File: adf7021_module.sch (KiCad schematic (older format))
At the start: 67 parts, among them J1 Conn_02x10_Counter_Clockwise, J2 Conn_Coaxial, J3 Conn_Coaxial, J4 Conn_02x10_Counter_Clockwise, U1 ADF7021, X1 19.68MHz

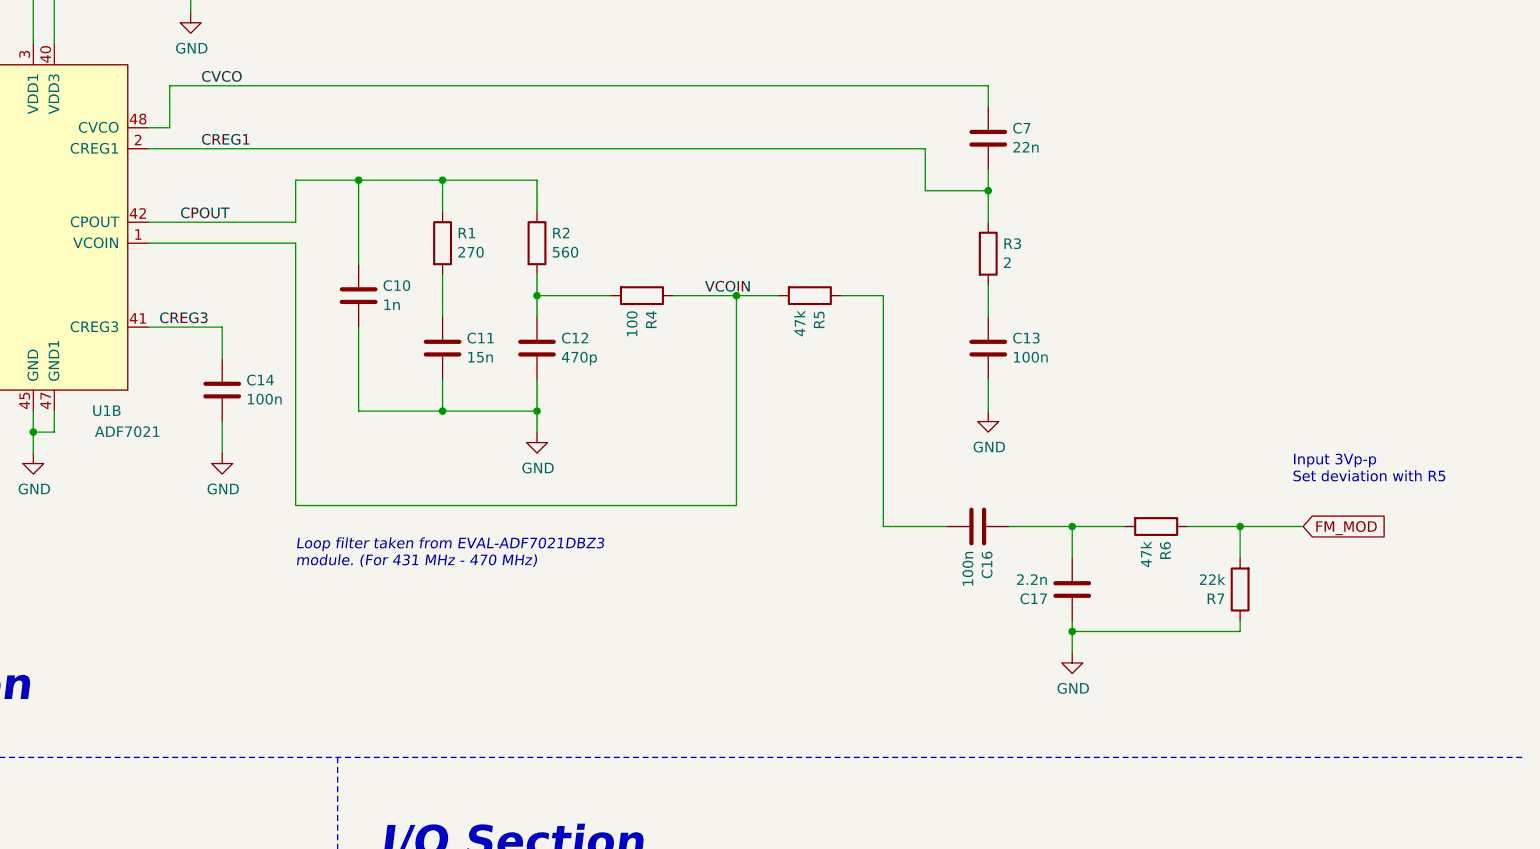
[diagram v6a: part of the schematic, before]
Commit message: Tidying up organization of FM Mod section
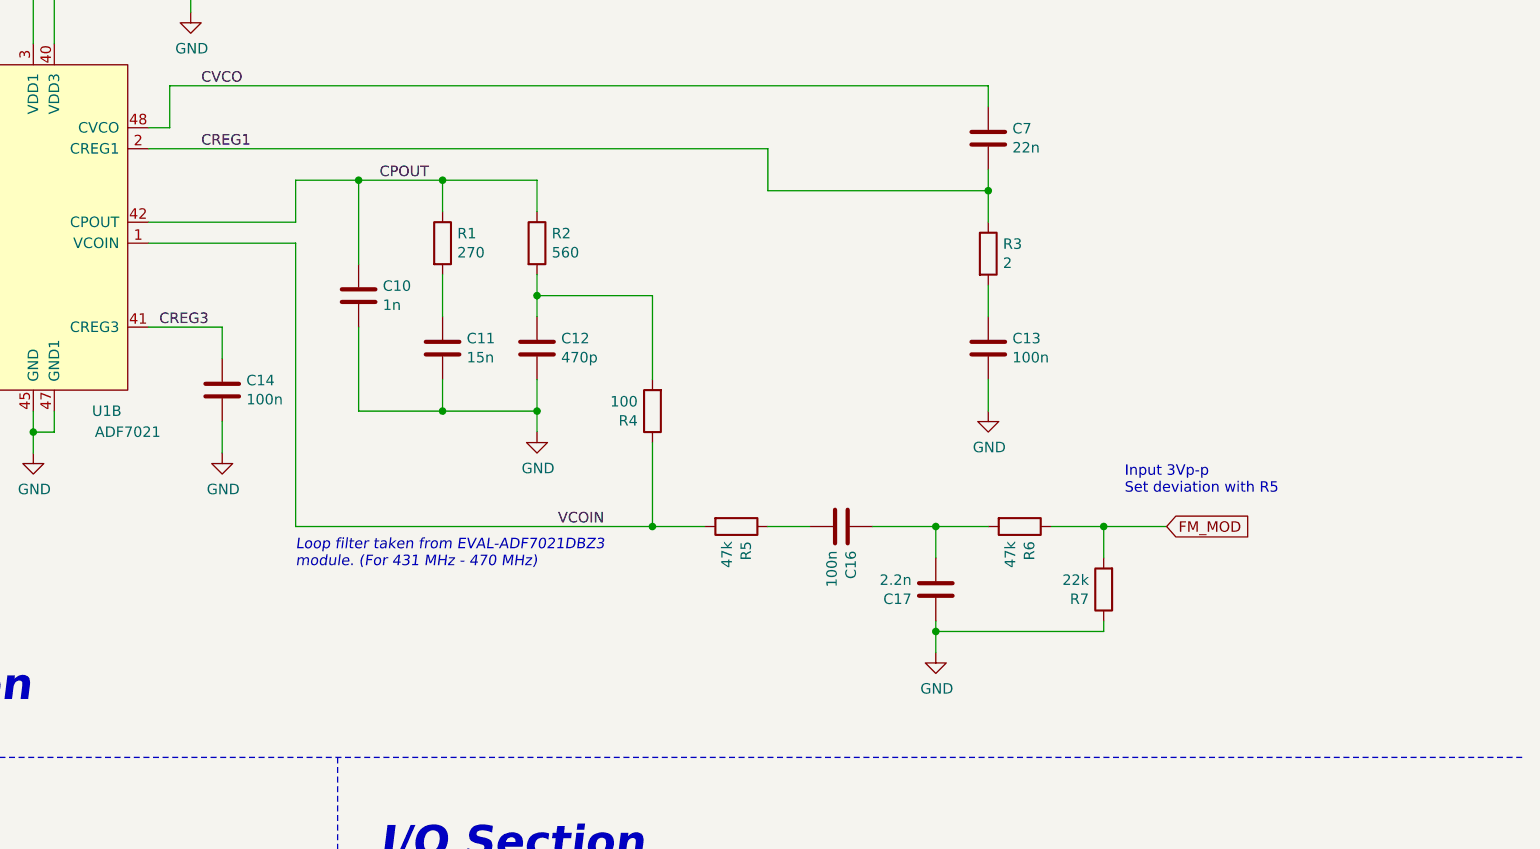
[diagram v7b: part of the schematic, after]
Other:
- moved on the sheet: C16, C17, R4, R5, R6, R7
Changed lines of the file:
@@
 	9200 3050 9900 3050
 Wire Wire Line
-	9900 3050 9900 4300
-Wire Wire Line
-	9900 4300 12000 4300
-Wire Wire Line
-	12000 4300 12000 3300
-Wire Wire Line
-	12000 3300 11700 3300
+	9900 3050 9900 4400
+Wire Wire Line
+	9900 4400 11600 4400
+Wire Wire Line
+	11600 4400 11600 4000
 Connection ~ 11050 3300
 Wire Wire Line
@@
 	9900 2750 10200 2750
 Connection ~ 10200 2750
-Text Label 9350 2950 0    50   ~ 0
+Text Label 10300 2750 0    50   ~ 0
 CPOUT
-Text Label 11850 3300 0    50   ~ 0
+Text Label 11150 4400 0    50   ~ 0
 VCOIN
 Text Label 9450 2300 0    50   ~ 0
@@
 	13200 2300 13200 2400
 Wire Wire Line
-	12900 2600 12900 2800
-Wire Wire Line
-	12900 2800 13200 2800
+	12150 2600 12150 2800
+Wire Wire Line
+	12150 2800 13200 2800
 Wire Wire Line
 	13200 2800 13200 2700
@@
 	9300 2300 13200 2300
 Wire Wire Line
-	9200 2600 12900 2600
+	9200 2600 12150 2600
 $Comp
 L Oscillator:DFA-S2 X?
@@
 L Device:R R?
 U 1 1 5FD0CAC2
-P 11550 3300
+P 11600 3850
 AR Path="/5FB73817/5FD0CAC2" Ref="R?"  Part="1"
 AR Path="/5FD0CAC2" Ref="R4"  Part="1"
-F 0 "R4" H 11620 3346 50  0000 L CNN
-F 1 "100" H 11620 3255 50  0000 L CNN
-F 2 "" V 11480 3300 50  0001 C CNN
-F 3 "~" H 11550 3300 50  0001 C CNN
-	1    11550 3300
-	0    1    1    0
-$EndComp
-Wire Wire Line
-	11400 3300 11050 3300
+F 0 "R4" H 11670 3896 50  0000 L CNN
+F 1 "100" H 11670 3805 50  0000 L CNN
+F 2 "" V 11530 3850 50  0001 C CNN
+F 3 "~" H 11600 3850 50  0001 C CNN
+	1    11600 3850
+	-1   0    0    1
+$EndComp
 $Comp
 L Device:R R?
 U 1 1 5FD0CF8B
-P 12350 3300
+P 12000 4400
 AR Path="/5FB73817/5FD0CF8B" Ref="R?"  Part="1"
 AR Path="/5FD0CF8B" Ref="R5"  Part="1"
-F 0 "R5" H 12420 3346 50  0000 L CNN
-F 1 "47k" H 12420 3255 50  0000 L CNN
-F 2 "" V 12280 3300 50  0001 C CNN
-F 3 "~" H 12350 3300 50  0001 C CNN
-	1    12350 3300
-	0    1    1    0
-$EndComp
-Wire Wire Line
-	12200 3300 12000 3300
-Connection ~ 12000 3300
-Wire Wire Line
-	12500 3300 12700 3300
-Wire Wire Line
-	12700 3300 12700 4400
-Wire Wire Line
-	12700 4400 13000 4400
+F 0 "R5" H 12070 4446 50  0000 L CNN
+F 1 "47k" H 12070 4355 50  0000 L CNN
+F 2 "" V 11930 4400 50  0001 C CNN
+F 3 "~" H 12000 4400 50  0001 C CNN
+	1    12000 4400
+	0    1    1    0
+$EndComp
+Wire Wire Line
+	11850 4400 11600 4400
 $Comp
 L Device:C C?
 U 1 1 5FD40884
-P 13150 4400
+P 12500 4400
 AR Path="/5FB73817/5FD40884" Ref="C?"  Part="1"
 AR Path="/5FD40884" Ref="C16"  Part="1"
-F 0 "C16" H 13265 4446 50  0000 L CNN
-F 1 "100n" H 13265 4355 50  0000 L CNN
-F 2 "" H 13188 4250 50  0001 C CNN
-F 3 "~" H 13150 4400 50  0001 C CNN
-	1    13150 4400
+F 0 "C16" H 12615 4446 50  0000 L CNN
+F 1 "100n" H 12615 4355 50  0000 L CNN
+F 2 "" H 12538 4250 50  0001 C CNN
+F 3 "~" H 12500 4400 50  0001 C CNN
+	1    12500 4400
 	0    1    1    0
 $EndComp
@@
 L Device:C C?
 U 1 1 5FD40D6A
-P 13600 4700
+P 12950 4700
 AR Path="/5FB73817/5FD40D6A" Ref="C?"  Part="1"
 AR Path="/5FD40D6A" Ref="C17"  Part="1"
-F 0 "C17" H 13715 4746 50  0000 L CNN
-F 1 "2.2n" H 13715 4655 50  0000 L CNN
-F 2 "" H 13638 4550 50  0001 C CNN
-F 3 "~" H 13600 4700 50  0001 C CNN
-	1    13600 4700
+F 0 "C17" H 13065 4746 50  0000 L CNN
+F 1 "2.2n" H 13065 4655 50  0000 L CNN
+F 2 "" H 12988 4550 50  0001 C CNN
+F 3 "~" H 12950 4700 50  0001 C CNN
+	1    12950 4700
 	-1   0    0    1
 $EndComp
@@
 L Device:R R?
 U 1 1 5FD41385
-P 14000 4400
+P 13350 4400
 AR Path="/5FB73817/5FD41385" Ref="R?"  Part="1"
 AR Path="/5FD41385" Ref="R6"  Part="1"
-F 0 "R6" H 14070 4446 50  0000 L CNN
-F 1 "47k" H 14070 4355 50  0000 L CNN
-F 2 "" V 13930 4400 50  0001 C CNN
-F 3 "~" H 14000 4400 50  0001 C CNN
-	1    14000 4400
+F 0 "R6" H 13420 4446 50  0000 L CNN
+F 1 "47k" H 13420 4355 50  0000 L CNN
+F 2 "" V 13280 4400 50  0001 C CNN
+F 3 "~" H 13350 4400 50  0001 C CNN
+	1    13350 4400
 	0    1    1    0
 $EndComp
@@
 L Device:R R?
 U 1 1 5FD41903
-P 14400 4700
+P 13750 4700
 AR Path="/5FB73817/5FD41903" Ref="R?"  Part="1"
 AR Path="/5FD41903" Ref="R7"  Part="1"
-F 0 "R7" H 14470 4746 50  0000 L CNN
-F 1 "22k" H 14470 4655 50  0000 L CNN
-F 2 "" V 14330 4700 50  0001 C CNN
-F 3 "~" H 14400 4700 50  0001 C CNN
-	1    14400 4700
+F 0 "R7" H 13820 4746 50  0000 L CNN
+F 1 "22k" H 13820 4655 50  0000 L CNN
+F 2 "" V 13680 4700 50  0001 C CNN
+F 3 "~" H 13750 4700 50  0001 C CNN
+	1    13750 4700
 	-1   0    0    1
 $EndComp
@@
 L power:GND #PWR?
 U 1 1 5FD41EDF
-P 13600 5000
+P 12950 5000
 AR Path="/5FB73817/5FD41EDF" Ref="#PWR?"  Part="1"
 AR Path="/5FD41EDF" Ref="#PWR017"  Part="1"
-F 0 "#PWR017" H 13600 4750 50  0001 C CNN
-F 1 "GND" H 13605 4827 50  0000 C CNN
-F 2 "" H 13600 5000 50  0001 C CNN
-F 3 "" H 13600 5000 50  0001 C CNN
-	1    13600 5000
-	1    0    0    -1
-$EndComp
-Wire Wire Line
-	13600 5000 13600 4900
-Wire Wire Line
-	13600 4900 14400 4900
-Wire Wire Line
-	14400 4900 14400 4850
-Connection ~ 13600 4900
-Wire Wire Line
-	13600 4900 13600 4850
-Wire Wire Line
-	13600 4550 13600 4400
-Wire Wire Line
-	13600 4400 13300 4400
-Wire Wire Line
-	13600 4400 13850 4400
-Connection ~ 13600 4400
-Wire Wire Line
-	14150 4400 14400 4400
-Wire Wire Line
-	14400 4400 14400 4550
-Wire Wire Line
-	14400 4400 14700 4400
-Connection ~ 14400 4400
-Text Notes 14650 4200 0    50   ~ 0
+F 0 "#PWR017" H 12950 4750 50  0001 C CNN
+F 1 "GND" H 12955 4827 50  0000 C CNN
+F 2 "" H 12950 5000 50  0001 C CNN
+F 3 "" H 12950 5000 50  0001 C CNN
+	1    12950 5000
+	1    0    0    -1
+$EndComp
+Wire Wire Line
+	12950 5000 12950 4900
+Wire Wire Line
+	12950 4900 13750 4900
+Wire Wire Line
+	13750 4900 13750 4850
+Connection ~ 12950 4900
+Wire Wire Line
+	12950 4900 12950 4850
+Wire Wire Line
+	12950 4550 12950 4400
+Wire Wire Line
+	12950 4400 12650 4400
+Wire Wire Line
+	12950 4400 13200 4400
+Connection ~ 12950 4400
+Wire Wire Line
+	13500 4400 13750 4400
+Wire Wire Line
+	13750 4400 13750 4550
+Wire Wire Line
+	13750 4400 14050 4400
+Connection ~ 13750 4400
+Text Notes 13850 4250 0    50   ~ 0
 Input 3Vp-p\nSet deviation with R5
 $Comp
@@
 Wire Wire Line
 	3450 3350 3600 3350
-Text GLabel 14700 4400 2    50   Input ~ 0
+Text GLabel 14050 4400 2    50   Input ~ 0
 FM_MOD
 Text Notes 2000 2900 0    30   ~ 0
@@
 Wire Wire Line
 	11400 7150 11550 7150
+Connection ~ 11600 4400
+Wire Wire Line
+	12150 4400 12350 4400
+Wire Wire Line
+	11600 3700 11600 3300
+Wire Wire Line
+	11050 3300 11600 3300
 $EndSCHEMATC

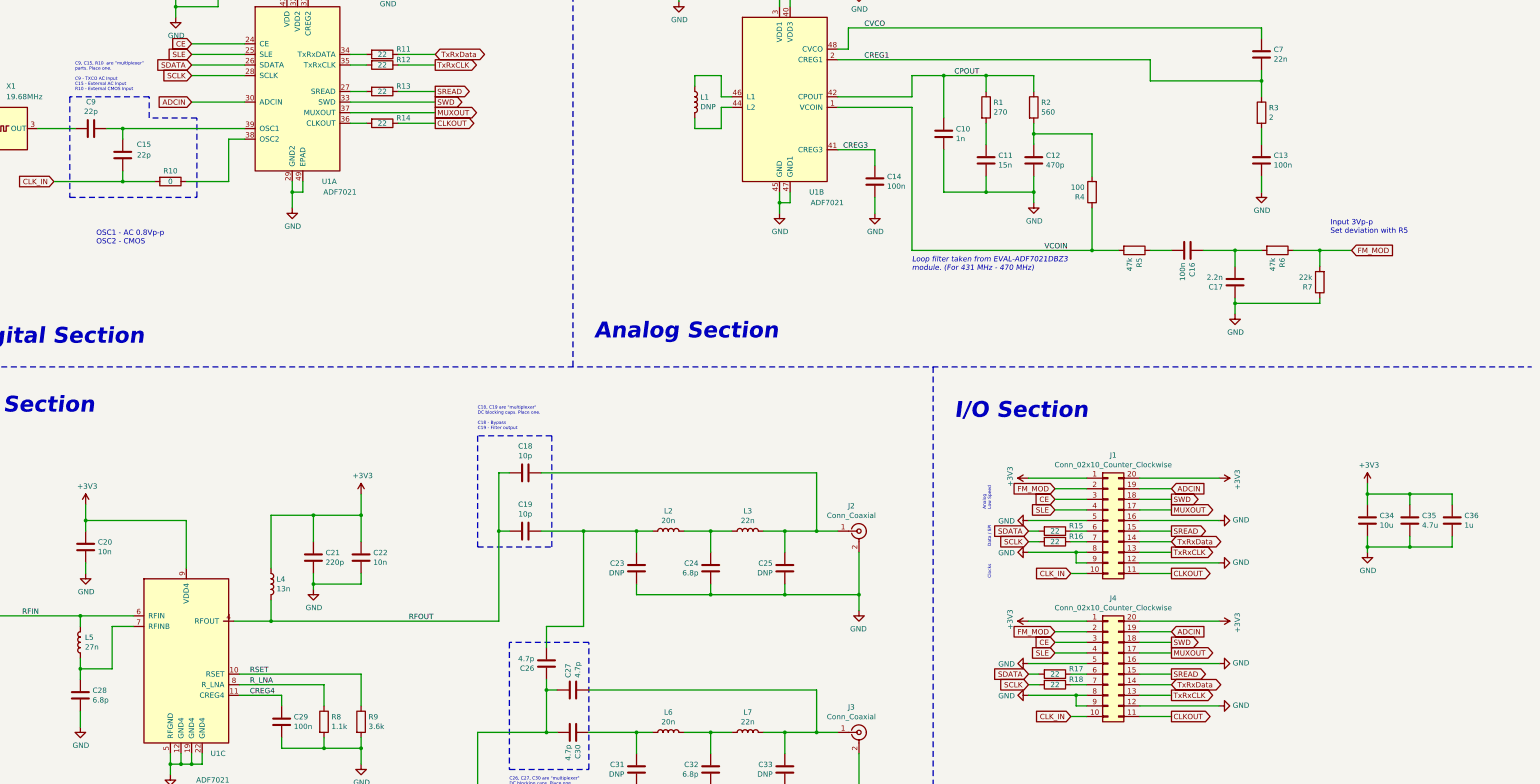
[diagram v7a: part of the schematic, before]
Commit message: Adding mounting holes
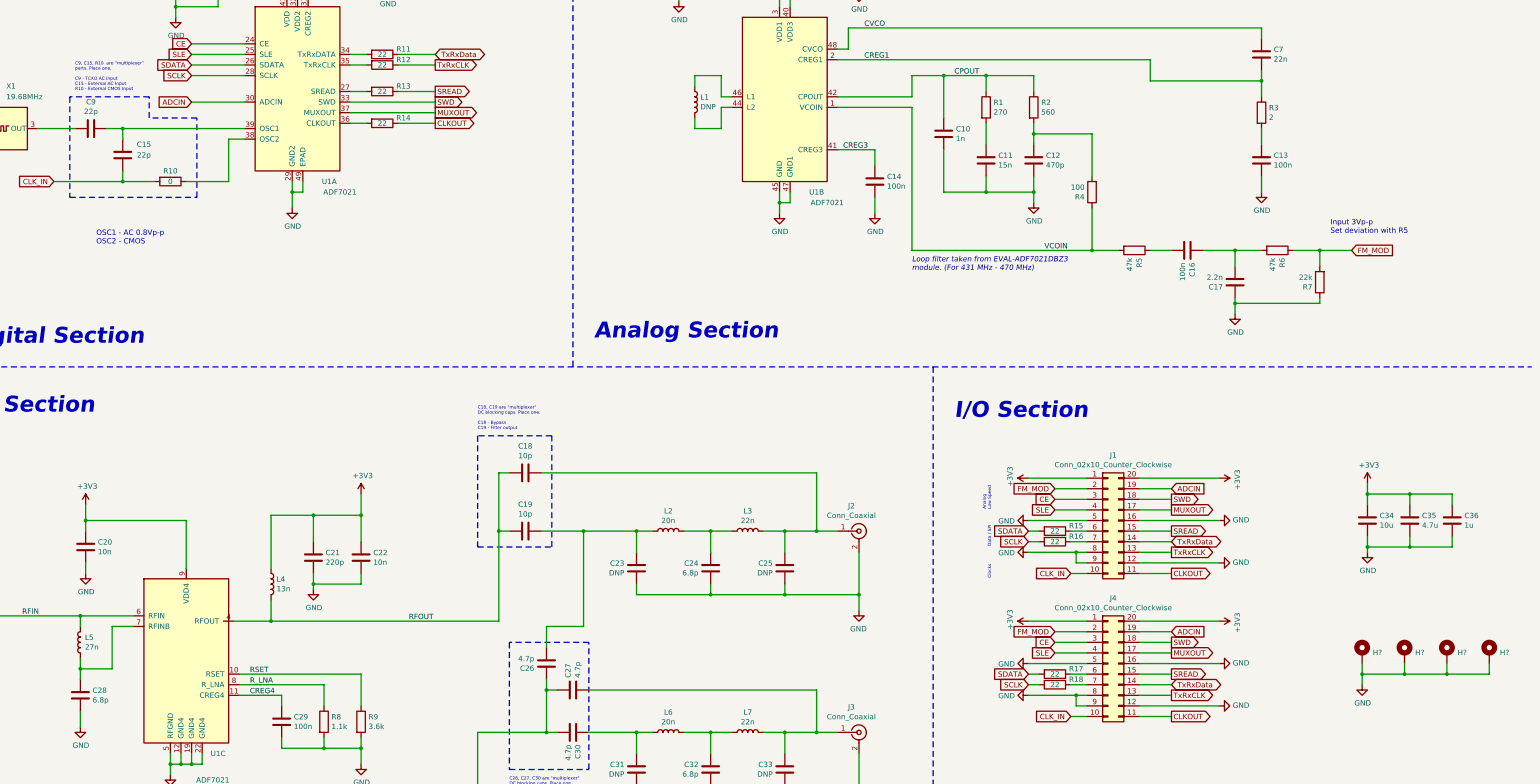
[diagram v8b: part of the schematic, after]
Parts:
- added H? (x4): MountingHole_Pad, symbol Mechanical:MountingHole_Pad
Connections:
- net GND: now also H?.1, H?.1, H?.1, H?.1
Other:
- note added: "C9, C15, R10 are "multiplexer"\nparts. Place one.\n\nC9 - TCXO AC Input\nC15 - External AC Input\nR10 - External CMOS Input"
- note removed: "C9, C15, R10 are "multiplexer"\nparts. Place one.\n\nC9 - TXCO AC Input\nC15 - External AC Input\nR10 - External CMOS Input"
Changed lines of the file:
@@
 FM_MOD
 Text Notes 2000 2900 0    30   ~ 0
-C9, C15, R10  are "multiplexer"\nparts. Place one.\n\nC9 - TXCO AC Input\nC15 - External AC Input\nR10 - External CMOS Input
+C9, C15, R10  are "multiplexer"\nparts. Place one.\n\nC9 - TCXO AC Input\nC15 - External AC Input\nR10 - External CMOS Input
 Wire Wire Line
 	1650 3250 2000 3250
@@
 Wire Wire Line
 	11050 3300 11600 3300
+$Comp
+L Mechanical:MountingHole_Pad H?
+U 1 1 608F38E7
+P 14150 8200
+F 0 "H?" H 14250 8203 50  0000 L CNN
+F 1 "MountingHole_Pad" H 14250 8158 50  0001 L CNN
+F 2 "" H 14150 8200 50  0001 C CNN
+F 3 "~" H 14150 8200 50  0001 C CNN
+	1    14150 8200
+	1    0    0    -1
+$EndComp
+$Comp
+L Mechanical:MountingHole_Pad H?
+U 1 1 608F437B
+P 14550 8200
+F 0 "H?" H 14650 8203 50  0000 L CNN
+F 1 "MountingHole_Pad" H 14650 8158 50  0001 L CNN
+F 2 "" H 14550 8200 50  0001 C CNN
+F 3 "~" H 14550 8200 50  0001 C CNN
+	1    14550 8200
+	1    0    0    -1
+$EndComp
+$Comp
+L Mechanical:MountingHole_Pad H?
+U 1 1 608F497B
+P 14950 8200
+F 0 "H?" H 15050 8203 50  0000 L CNN
+F 1 "MountingHole_Pad" H 15050 8158 50  0001 L CNN
+F 2 "" H 14950 8200 50  0001 C CNN
+F 3 "~" H 14950 8200 50  0001 C CNN
+	1    14950 8200
+	1    0    0    -1
+$EndComp
+$Comp
+L Mechanical:MountingHole_Pad H?
+U 1 1 608F4F4D
+P 15350 8200
+F 0 "H?" H 15450 8203 50  0000 L CNN
+F 1 "MountingHole_Pad" H 15450 8158 50  0001 L CNN
+F 2 "" H 15350 8200 50  0001 C CNN
+F 3 "~" H 15350 8200 50  0001 C CNN
+	1    15350 8200
+	1    0    0    -1
+$EndComp
+$Comp
+L power:GND #PWR?
+U 1 1 608F5BFE
+P 14150 8500
+F 0 "#PWR?" H 14150 8250 50  0001 C CNN
+F 1 "GND" H 14155 8327 50  0000 C CNN
+F 2 "" H 14150 8500 50  0001 C CNN
+F 3 "" H 14150 8500 50  0001 C CNN
+	1    14150 8500
+	1    0    0    -1
+$EndComp
+Wire Wire Line
+	14150 8500 14150 8400
+Wire Wire Line
+	14150 8400 14550 8400
+Wire Wire Line
+	15350 8400 15350 8300
+Connection ~ 14150 8400
+Wire Wire Line
+	14150 8400 14150 8300
+Wire Wire Line
+	14950 8300 14950 8400
+Connection ~ 14950 8400
+Wire Wire Line
+	14950 8400 15350 8400
+Wire Wire Line
+	14550 8300 14550 8400
+Connection ~ 14550 8400
+Wire Wire Line
+	14550 8400 14950 8400
 $EndSCHEMATC
